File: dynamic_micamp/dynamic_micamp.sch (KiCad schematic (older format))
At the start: 23 parts, among them J1 AudioJack3, J2 Jack-DC, J3 AudioJack3, U1 NJM4580, U2 L7805, U3 NJM4580

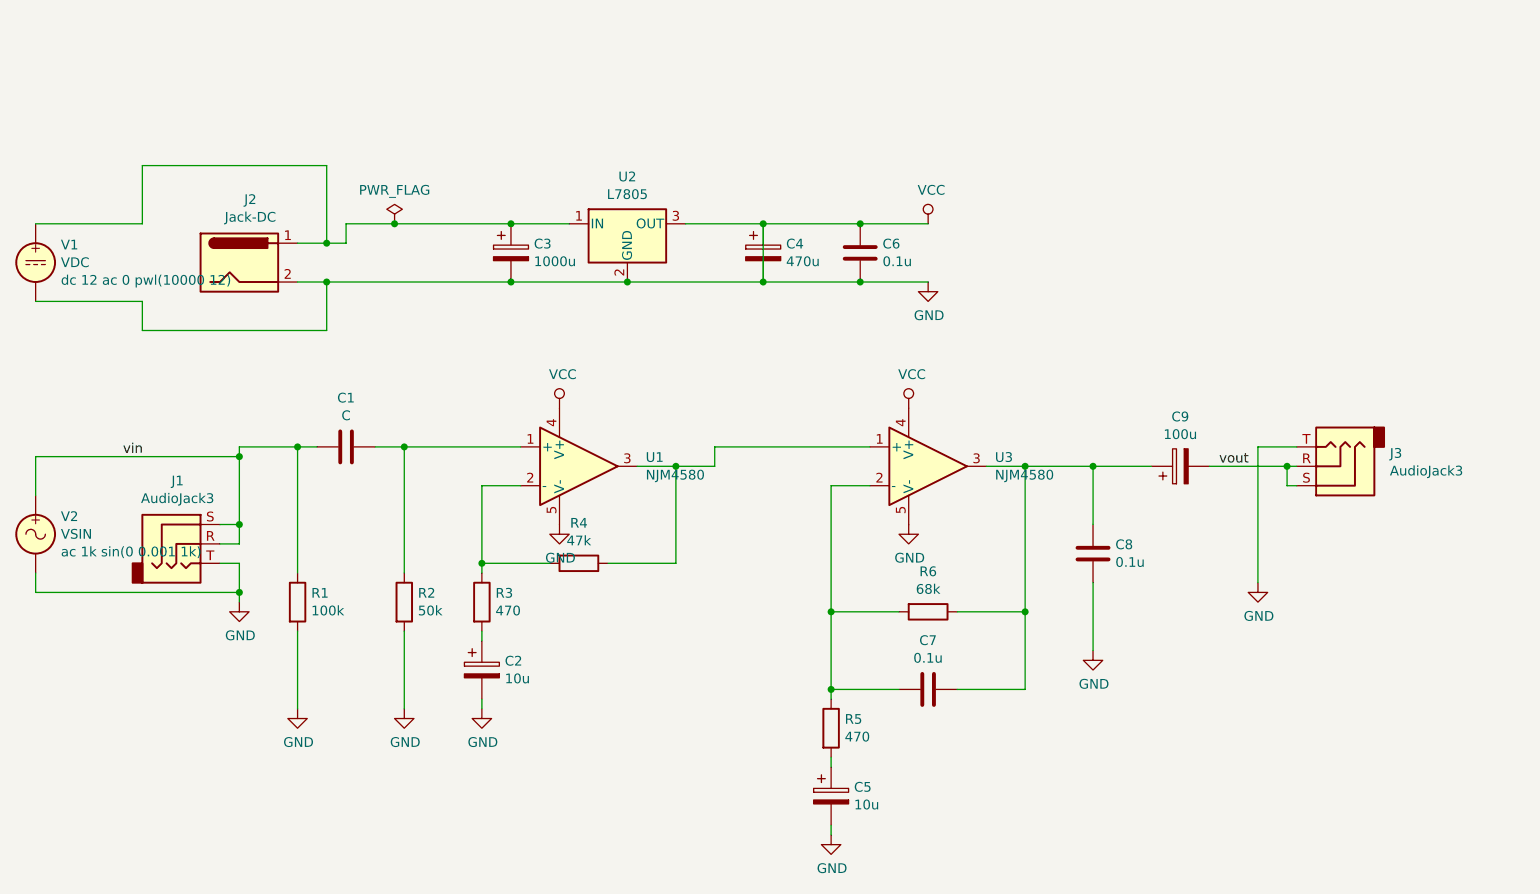
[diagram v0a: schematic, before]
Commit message: constants are fixed using LTSpice simulation
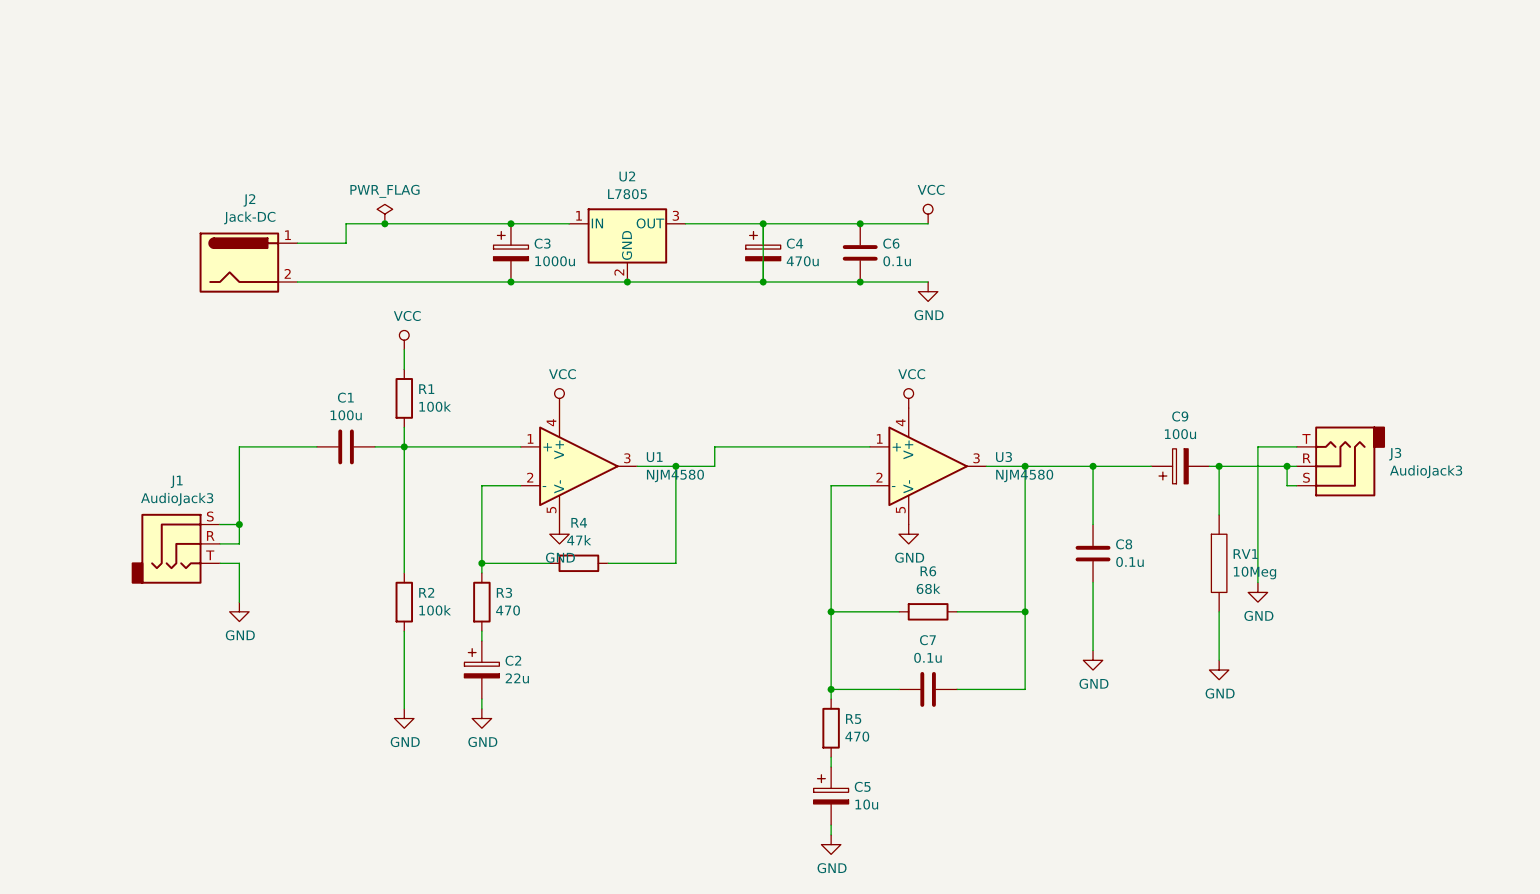
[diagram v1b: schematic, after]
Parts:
- removed V1: VDC, symbol Simulation_SPICE:VDC
- removed V2: VSIN, symbol Simulation_SPICE:VSIN
- added RV1: 10Meg, symbol pspice:R
- C1: value C -> 100u
- C2: value 10u -> 22u
- R2: value 50k -> 100k
- U1, U3: Spice_Lib_File cadlab.lib -> njm4580_v2.lib; Spice_Model LM318 -> njm4580_s
- U2: Spice_Lib_File cadlab.lib -> lm78xx.lib; Spice_Model lm7805C -> LM7805
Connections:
- net GND: now also R1.1, RV1.2; no longer R1.2
- net at C1.1, R2.1, U1.1 (+): now also R1.2
- net vin: no longer names the net of C1.2, J1.R, J1.S
- net vin: no longer R1.1
- net vout: no longer names the net of C9.2, J3.R, J3.S
- net vout: now also RV1.1
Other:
- moved on the sheet: R1
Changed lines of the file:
@@
-$EndComp
-$Comp
-L Regulator_Linear:L7805 U2
-U 1 1 5EFC8F35
-P 3250 1850
-F 0 "U2" H 3250 2092 50  0000 C CNN
-F 1 "L7805" H 3250 2001 50  0000 C CNN
-F 2 "" H 3275 1700 50  0001 L CIN
-F 3 "http://www.st.com/content/ccc/resource/technical/document/datasheet/41/4f/b3/b0/12/d4/47/88/CD00000444.pdf/files/CD00000444.pdf/jcr:content/translations/en.CD00000444.pdf" H 3250 1800 50  0001 C CNN
-F 4 "X" H 3250 1850 50  0001 C CNN "Spice_Primitive"
-F 5 "lm7805C" H 3250 1850 50  0001 C CNN "Spice_Model"
-F 6 "Y" H 3250 1850 50  0001 C CNN "Spice_Netlist_Enabled"
-F 7 "cadlab.lib" H 3250 1850 50  0001 C CNN "Spice_Lib_File"
-	1    3250 1850
-	1    0    0    -1
 $EndComp
 $Comp
@@
 $EndComp
 Wire Wire Line
-	1550 1950 1700 1950
-Wire Wire Line
 	1800 1950 1800 1850
-Wire Wire Line
-	1800 1850 2050 1850
 Wire Wire Line
 	2950 1850 2650 1850
@@
 	3250 2150 2650 2150
 Connection ~ 2650 2150
-Wire Wire Line
-	3250 2150 3950 2150
-Connection ~ 3250 2150
 $Comp
 L Device:C C6
@@
 $EndComp
 Wire Wire Line
-	3950 1850 4450 1850
-Connection ~ 3950 1850
-Wire Wire Line
 	3950 1850 3950 2150
-Connection ~ 4450 1850
 Wire Wire Line
 	4450 1850 4800 1850
@@
 	4450 2150 4800 2150
 Connection ~ 4450 2150
-$Comp
-L power:VCC #PWR06
-U 1 1 5EFCFCE7
-P 4800 1850
-F 0 "#PWR06" H 4800 1700 50  0001 C CNN
-F 1 "VCC" H 4817 2023 50  0000 C CNN
-F 2 "" H 4800 1850 50  0001 C CNN
-F 3 "" H 4800 1850 50  0001 C CNN
-	1    4800 1850
-	1    0    0    -1
-$EndComp
 $Comp
 L power:GND #PWR07
@@
 	1    0    0    -1
 $EndComp
-$Comp
-L power:PWR_FLAG #FLG01
-U 1 1 5EFD11B4
-P 2050 1850
-F 0 "#FLG01" H 2050 1925 50  0001 C CNN
-F 1 "PWR_FLAG" H 2050 2023 50  0000 C CNN
-F 2 "" H 2050 1850 50  0001 C CNN
-F 3 "~" H 2050 1850 50  0001 C CNN
-	1    2050 1850
-	1    0    0    -1
-$EndComp
-Connection ~ 2050 1850
-Wire Wire Line
-	2050 1850 2650 1850
 $Comp
 L Connector:AudioJack3 J1
@@
 	1150 3600 1250 3600
 Wire Wire Line
-	1250 3600 1250 3750
-Wire Wire Line
 	1150 3400 1250 3400
-Wire Wire Line
-	1250 3400 1250 3050
 Wire Wire Line
 	1150 3500 1250 3500
@@
 P 1800 3000
 F 0 "C1" V 1548 3000 50  0000 C CNN
-F 1 "C" V 1639 3000 50  0000 C CNN
+F 1 "100u" V 1639 3000 50  0000 C CNN
 F 2 "" H 1838 2850 50  0001 C CNN
 F 3 "~" H 1800 3000 50  0001 C CNN
 	1    1800 3000
 	0    1    1    0
-$EndComp
-Wire Wire Line
-	1250 3000 1550 3000
-Wire Wire Line
-	1550 3000 1550 3650
-Connection ~ 1550 3000
-Wire Wire Line
-	1550 3000 1650 3000
-$Comp
-L Device:R R1
-U 1 1 5EFF6AD7
-P 1550 3800
-F 0 "R1" H 1620 3846 50  0000 L CNN
-F 1 "100k" H 1620 3755 50  0000 L CNN
-F 2 "" V 1480 3800 50  0001 C CNN
-F 3 "~" H 1550 3800 50  0001 C CNN
-	1    1550 3800
-	1    0    0    -1
-$EndComp
-Wire Wire Line
-	1550 3950 1550 4350
-$Comp
-L power:GND #PWR02
-U 1 1 5EFF79E3
-P 1550 4350
-F 0 "#PWR02" H 1550 4100 50  0001 C CNN
-F 1 "GND" H 1555 4177 50  0000 C CNN
-F 2 "" H 1550 4350 50  0001 C CNN
-F 3 "" H 1550 4350 50  0001 C CNN
-	1    1550 4350
-	1    0    0    -1
 $EndComp
 Wire Wire Line
@@
 P 2100 3800
 F 0 "R2" H 2170 3846 50  0000 L CNN
-F 1 "50k" H 2170 3755 50  0000 L CNN
+F 1 "100k" H 2170 3755 50  0000 L CNN
 F 2 "" V 2030 3800 50  0001 C CNN
 F 3 "~" H 2100 3800 50  0001 C CNN
@@
 P 2500 4150
 F 0 "C2" H 2618 4196 50  0000 L CNN
-F 1 "10u" H 2618 4105 50  0000 L CNN
+F 1 "22u" H 2618 4105 50  0000 L CNN
 F 2 "" H 2538 4000 50  0001 C CNN
 F 3 "~" H 2500 4150 50  0001 C CNN
@@
 	6500 3000 6500 3700
 Wire Wire Line
-	6250 3100 6650 3100
+	6250 3100 6300 3100
 Wire Wire Line
 	6650 3100 6650 3200
@@
 	1    0    0    -1
 $EndComp
-Wire Wire Line
-	3550 1850 3950 1850
-Wire Wire Line
-	1550 2150 1700 2150
-Wire Wire Line
-	750  1550 1700 1550
-Wire Wire Line
-	1700 1550 1700 1950
-Connection ~ 1700 1950
-Wire Wire Line
-	1700 1950 1800 1950
-Wire Wire Line
-	750  2400 1700 2400
-Wire Wire Line
-	1700 2400 1700 2150
-Connection ~ 1700 2150
-Wire Wire Line
-	1700 2150 2650 2150
-$Comp
-L Simulation_SPICE:VSIN V2
-U 1 1 5F036F2A
-P 200 3450
-F 0 "V2" H 330 3541 50  0000 L CNN
-F 1 "VSIN" H 330 3450 50  0000 L CNN
-F 2 "" H 200 3450 50  0001 C CNN
-F 3 "~" H 200 3450 50  0001 C CNN
-F 4 "Y" H 200 3450 50  0001 L CNN "Spice_Netlist_Enabled"
-F 5 "V" H 200 3450 50  0001 L CNN "Spice_Primitive"
-F 6 "ac 1k sin(0 0.001 1k)" H 330 3359 50  0000 L CNN "Spice_Model"
-	1    200  3450
-	1    0    0    -1
-$EndComp
-Wire Wire Line
-	200  3650 200  3750
-Wire Wire Line
-	200  3750 1250 3750
-Connection ~ 1250 3750
-Wire Wire Line
-	1250 3750 1250 3800
-Wire Wire Line
-	200  3250 200  3050
-Wire Wire Line
-	200  3050 1250 3050
-Connection ~ 1250 3050
-Wire Wire Line
-	1250 3050 1250 3000
-$Comp
-L Simulation_SPICE:VDC V1
-U 1 1 5F03DC17
-P 200 2050
-F 0 "V1" H 330 2141 50  0000 L CNN
-F 1 "VDC" H 330 2050 50  0000 L CNN
-F 2 "" H 200 2050 50  0001 C CNN
-F 3 "~" H 200 2050 50  0001 C CNN
-F 4 "Y" H 200 2050 50  0001 L CNN "Spice_Netlist_Enabled"
-F 5 "V" H 200 2050 50  0001 L CNN "Spice_Primitive"
-F 6 "dc 12 ac 0 pwl(10000 12)" H 330 1959 50  0000 L CNN "Spice_Model"
-	1    200  2050
-	1    0    0    -1
-$EndComp
-Wire Wire Line
-	200  1850 750  1850
-Wire Wire Line
-	750  1550 750  1850
-Wire Wire Line
-	200  2250 750  2250
-Wire Wire Line
-	750  2250 750  2400
-Text Label 650  3050 0    50   ~ 0
-vin
-Text Label 6300 3100 0    50   ~ 0
-vout
 $Comp
 L Simulation_SPICE:OPAMP U1
@@
 F 4 "Y" H 3000 3100 50  0001 L CNN "Spice_Netlist_Enabled"
 F 5 "X" H 3000 3100 50  0001 L CNN "Spice_Primitive"
-F 6 "LM318" H 3000 3100 50  0001 C CNN "Spice_Model"
-F 7 "cadlab.lib" H 3000 3100 50  0001 C CNN "Spice_Lib_File"
+F 6 "njm4580_s" H 3000 3100 50  0001 C CNN "Spice_Model"
+F 7 "njm4580_v2.lib" H 3000 3100 50  0001 C CNN "Spice_Lib_File"
 F 8 "1 2 4 5 3" H 3000 3100 50  0001 C CNN "Spice_Node_Sequence"
 	1    3000 3100
@@
 F 4 "Y" H 4800 3100 50  0001 L CNN "Spice_Netlist_Enabled"
 F 5 "X" H 4800 3100 50  0001 L CNN "Spice_Primitive"
-F 6 "LM318" H 4800 3100 50  0001 C CNN "Spice_Model"
-F 7 "cadlab.lib" H 4800 3100 50  0001 C CNN "Spice_Lib_File"
+F 6 "njm4580_s" H 4800 3100 50  0001 C CNN "Spice_Model"
+F 7 "njm4580_v2.lib" H 4800 3100 50  0001 C CNN "Spice_Lib_File"
 F 8 "1 2 4 5 3" H 4800 3100 50  0001 C CNN "Spice_Node_Sequence"
 	1    4800 3100
@@
 	1    0    0    -1
 $EndComp
+$Comp
+L pspice:R RV1
+U 1 1 5EFF5423
+P 6300 3600
+F 0 "RV1" H 6368 3646 50  0000 L CNN
+F 1 "10Meg" H 6368 3555 50  0000 L CNN
+F 2 "" H 6300 3600 50  0001 C CNN
+F 3 "~" H 6300 3600 50  0001 C CNN
+	1    6300 3600
+	1    0    0    -1
+$EndComp
+Wire Wire Line
+	6300 3100 6300 3350
+Connection ~ 6300 3100
+Wire Wire Line
+	6300 3100 6650 3100
+Wire Wire Line
+	6300 3850 6300 4100
+$Comp
+L power:GND #PWR0101
+U 1 1 5EFF975B
+P 6300 4100
+F 0 "#PWR0101" H 6300 3850 50  0001 C CNN
+F 1 "GND" H 6305 3927 50  0000 C CNN
+F 2 "" H 6300 4100 50  0001 C CNN
+F 3 "" H 6300 4100 50  0001 C CNN
+	1    6300 4100
+	1    0    0    -1
+$EndComp
+Connection ~ 4450 1850
+Wire Wire Line
+	3550 1850 3950 1850
+Wire Wire Line
+	3950 1850 4450 1850
+Connection ~ 3950 1850
+Connection ~ 3250 2150
+Wire Wire Line
+	3250 2150 3950 2150
+$Comp
+L Regulator_Linear:L7805 U2
+U 1 1 5EFC8F35
+P 3250 1850
+F 0 "U2" H 3250 2092 50  0000 C CNN
+F 1 "L7805" H 3250 2001 50  0000 C CNN
+F 2 "" H 3275 1700 50  0001 L CIN
+F 3 "http://www.st.com/content/ccc/resource/technical/document/datasheet/41/4f/b3/b0/12/d4/47/88/CD00000444.pdf/files/CD00000444.pdf/jcr:content/translations/en.CD00000444.pdf" H 3250 1800 50  0001 C CNN
+F 4 "X" H 3250 1850 50  0001 C CNN "Spice_Primitive"
+F 5 "LM7805" H 3250 1850 50  0001 C CNN "Spice_Model"
+F 6 "Y" H 3250 1850 50  0001 C CNN "Spice_Netlist_Enabled"
+F 7 "lm78xx.lib" H 3250 1850 50  0001 C CNN "Spice_Lib_File"
+	1    3250 1850
+	1    0    0    -1
+$EndComp
+$Comp
+L power:VCC #PWR06
+U 1 1 5EFCFCE7
+P 4800 1850
+F 0 "#PWR06" H 4800 1700 50  0001 C CNN
+F 1 "VCC" H 4817 2023 50  0000 C CNN
+F 2 "" H 4800 1850 50  0001 C CNN
+F 3 "" H 4800 1850 50  0001 C CNN
+	1    4800 1850
+	1    0    0    -1
+$EndComp
+Wire Wire Line
+	1800 1850 2000 1850
+Wire Wire Line
+	1250 3000 1650 3000
+$Comp
+L Device:R R1
+U 1 1 5EFF6AD7
+P 2100 2750
+F 0 "R1" H 2170 2796 50  0000 L CNN
+F 1 "100k" H 2170 2705 50  0000 L CNN
+F 2 "" V 2030 2750 50  0001 C CNN
+F 3 "~" H 2100 2750 50  0001 C CNN
+	1    2100 2750
+	1    0    0    -1
+$EndComp
+Wire Wire Line
+	2100 2900 2100 3000
+Wire Wire Line
+	2100 2600 2100 2500
+$Comp
+L power:VCC #PWR02
+U 1 1 5F0130B3
+P 2100 2500
+F 0 "#PWR02" H 2100 2350 50  0001 C CNN
+F 1 "VCC" H 2117 2673 50  0000 C CNN
+F 2 "" H 2100 2500 50  0001 C CNN
+F 3 "" H 2100 2500 50  0001 C CNN
+	1    2100 2500
+	1    0    0    -1
+$EndComp
+Wire Wire Line
+	1550 2150 2650 2150
+Wire Wire Line
+	1550 1950 1800 1950
+Wire Wire Line
+	1250 3600 1250 3800
+Wire Wire Line
+	1250 3000 1250 3400
+$Comp
+L power:PWR_FLAG #FLG01
+U 1 1 5F014817
+P 2000 1850
+F 0 "#FLG01" H 2000 1925 50  0001 C CNN
+F 1 "PWR_FLAG" H 2000 2023 50  0000 C CNN
+F 2 "" H 2000 1850 50  0001 C CNN
+F 3 "~" H 2000 1850 50  0001 C CNN
+	1    2000 1850
+	1    0    0    -1
+$EndComp
+Connection ~ 2000 1850
+Wire Wire Line
+	2000 1850 2650 1850
 $EndSCHEMATC

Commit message: place footprints
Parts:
- removed J1, J3: AudioJack3, symbol Connector:AudioJack3
- removed J2: Jack-DC, symbol Connector:Jack-DC
- removed RV1: 10Meg, symbol pspice:R
- removed U1, U3: NJM4580, symbol Simulation_SPICE:OPAMP
- removed U2: L7805, symbol Regulator_Linear:L7805
- added J1, J3: AudioJack3_123, Connector_PinSocket_2.54mm:PinSocket_1x03_P2.54mm_Vertical, symbol Connector:AudioJack3_123
- added J2: USB_B_Micro, Connector_USB:USB_Micro-B_KOZEEY, symbol Connector:USB_B_Micro
- added L1: 220u, Inductor_THT:L_Axial_L5.3mm_D2.2mm_P7.62mm_Horizontal_Vishay_IM-1, symbol pspice:INDUCTOR
- added U1: NJM4580, Package_DIP:DIP-8_W7.62mm, symbol Amplifier_Operational:NJM4580
- C1: footprint (none) -> Capacitor_THT:C_Rect_L4.6mm_W4.6mm_P2.50mm_MKS02_FKP02
- C2: value 22u -> 10u; footprint (none) -> Capacitor_THT:CP_Radial_D5.0mm_P2.50mm
- C3: value 1000u -> 3300u; footprint (none) -> Capacitor_THT:CP_Radial_D10.0mm_P2.50mm
- C4: footprint (none) -> Capacitor_THT:CP_Radial_D10.0mm_P2.50mm
- C5: value 10u -> 0.1u; footprint (none) -> Capacitor_THT:C_Rect_L13.0mm_W3.0mm_P10.00mm_FKS3_FKP3_MKS4
- C6, C8: footprint (none) -> Capacitor_THT:C_Disc_D3.0mm_W1.6mm_P2.50mm
- C7: footprint (none) -> Capacitor_THT:C_Rect_L13.0mm_W3.0mm_P10.00mm_FKS3_FKP3_MKS4
- C9: footprint (none) -> Capacitor_THT:CP_Radial_D5.0mm_P2.50mm
- R1, R2, R3, R4, R5, R6: footprint (none) -> Resistor_THT:R_Axial_DIN0204_L3.6mm_D1.6mm_P5.08mm_Horizontal
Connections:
- net GND: now also J1.3, J2.5 (GND), J2.6 (Shield), J3.3, U1.4 (V-); no longer C4.1, C6.1, R1.1
- net VCC: now reaches C3.1
- net VCC: now also C4.1, C6.1, R1.1, L1.2, U1.8 (V+)
- net at C1.2: now also J1.1, J1.2
- net at C1.1, R1.2, R2.1: now also U1.3 (+)
- net at R3.1, R4.2: now also U1.2 (-)
- net at R4.1: now also U1.1, U1.5 (+)
- net at C9.2: now also J3.1, J3.2
- net at C7.1, C8.1, C9.1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: now also U1.7
- net at C7.2, R5.1, R6.2: now also U1.6 (-)
- new net: J2.1 (VBUS), L1.1
- no-connect marks 0 -> 3

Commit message: resize C3 to learger one
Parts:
- C3: footprint Capacitor_THT:CP_Radial_D10.0mm_P2.50mm -> Capacitor_THT:CP_Radial_D18.0mm_P7.50mm
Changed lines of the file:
@@
 F 0 "C3" H 3918 1346 50  0000 L CNN
 F 1 "3300u" H 3918 1255 50  0000 L CNN
-F 2 "Capacitor_THT:CP_Radial_D10.0mm_P2.50mm" H 3838 1150 50  0001 C CNN
+F 2 "Capacitor_THT:CP_Radial_D18.0mm_P7.50mm" H 3838 1150 50  0001 C CNN
 F 3 "~" H 3800 1300 50  0001 C CNN
 	1    3800 1300
